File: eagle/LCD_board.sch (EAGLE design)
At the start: 5 parts, among them CN1 1X4-CLEANBIG

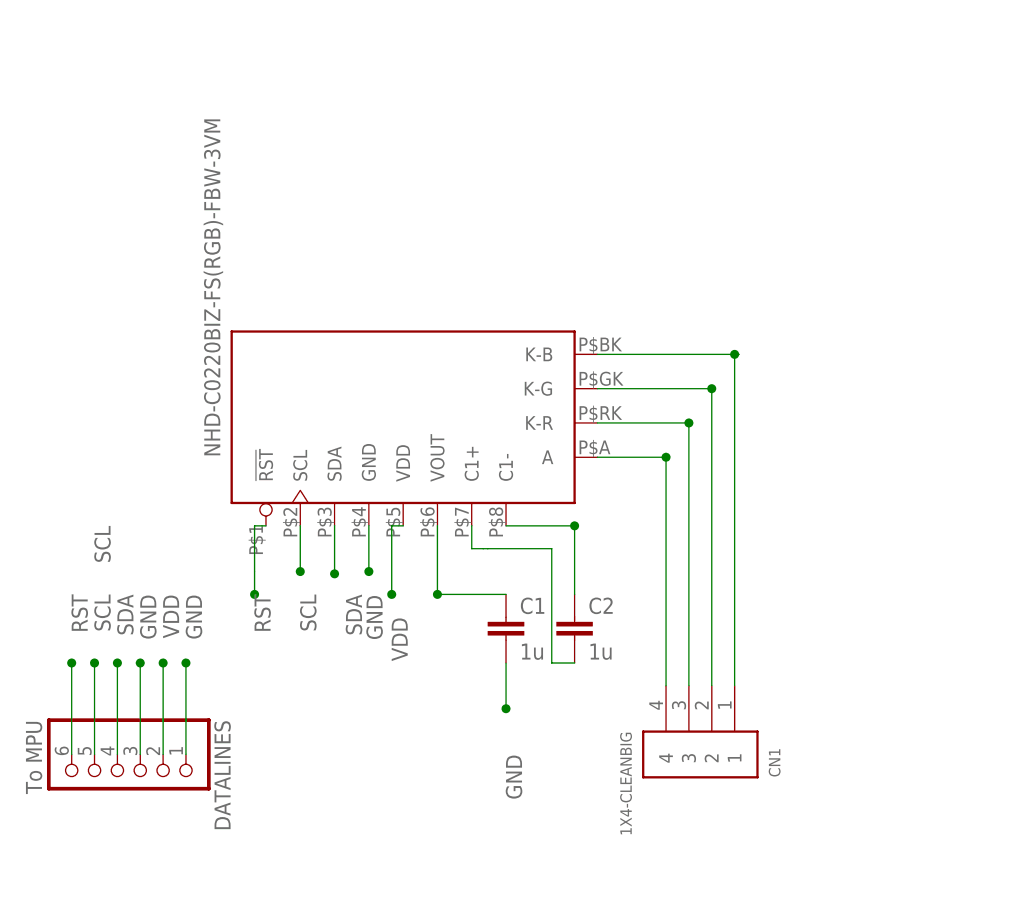
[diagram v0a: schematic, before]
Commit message: Moved ARGB pins on LCD screen schematic to match physical location. This should solve issue #9. Updated LCD_board.sch to reflect these changes.
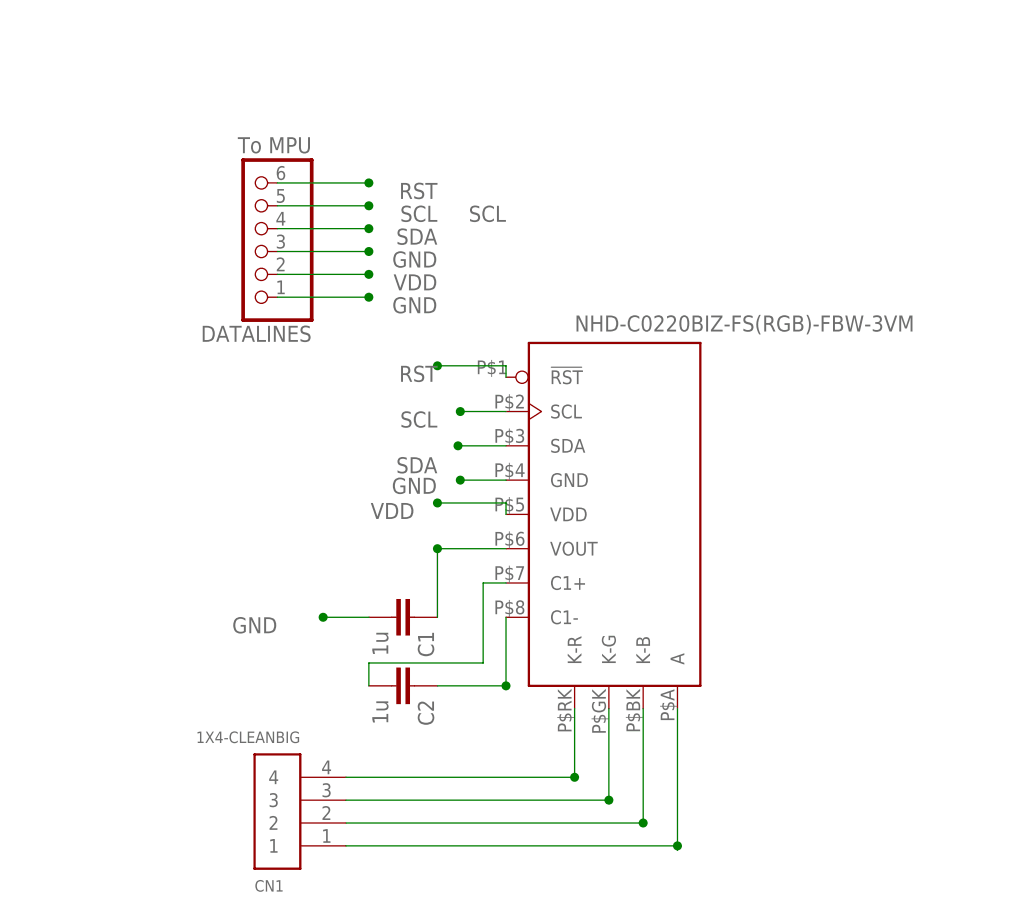
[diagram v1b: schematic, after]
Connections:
- net A: now also U$1.K-R; no longer U$1.A
- net GK: now also U$1.K-B; no longer U$1.K-G
- net N$2: now also U$1.K-G; no longer U$1.K-R
- net N$4: now also U$1.A; no longer U$1.K-B
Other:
- moved on the sheet: C1, C2, CN1, DATALINES
